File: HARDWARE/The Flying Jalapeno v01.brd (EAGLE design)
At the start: 73.7 x 52.1 mm, 80 parts, among them J1 ., J2 7V, Q1 16MHZ, Q3 P-Channel MOSFET, U2 ATMEGA328P_TQFP

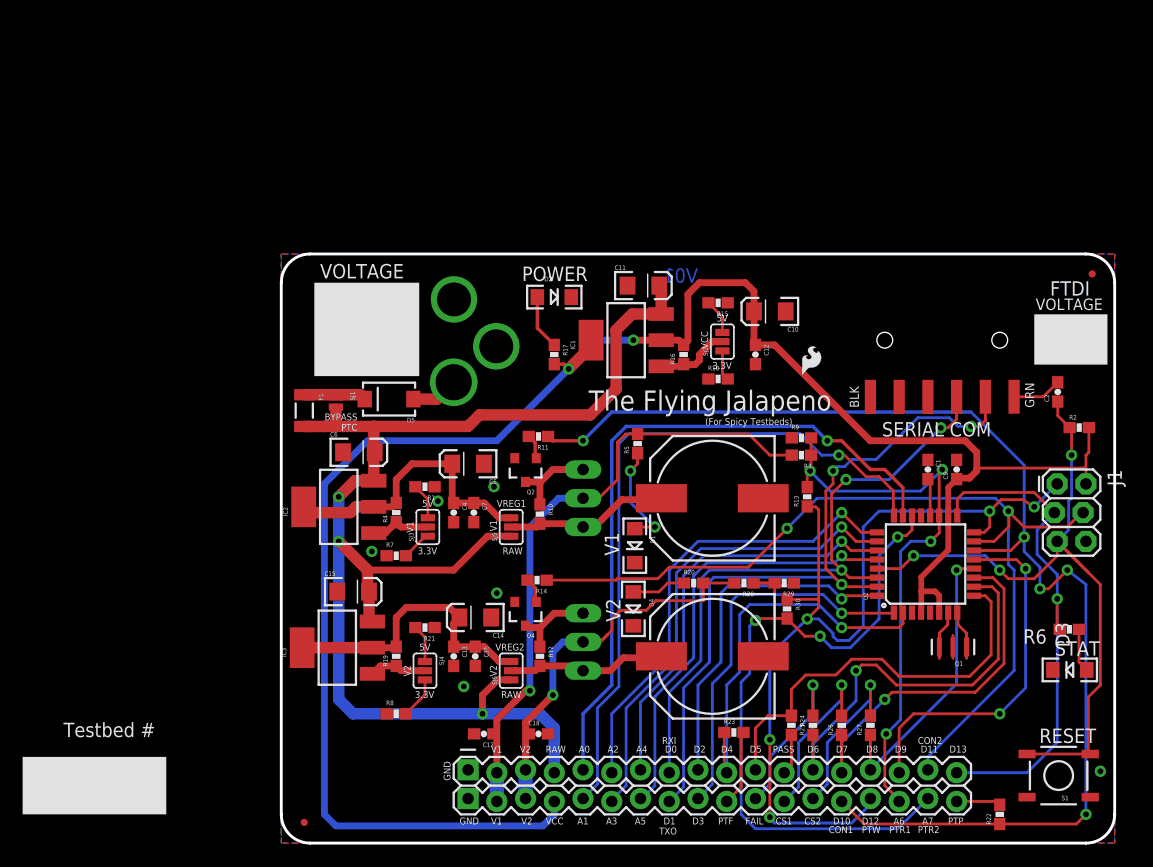
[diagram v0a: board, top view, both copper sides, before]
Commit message: Moved to Mega2560 and 2x30 2mm connector
device and packages for the 2x30 connector all live in the "local"
sparkfun.lbr for now. I will push to testing.lbr soon.
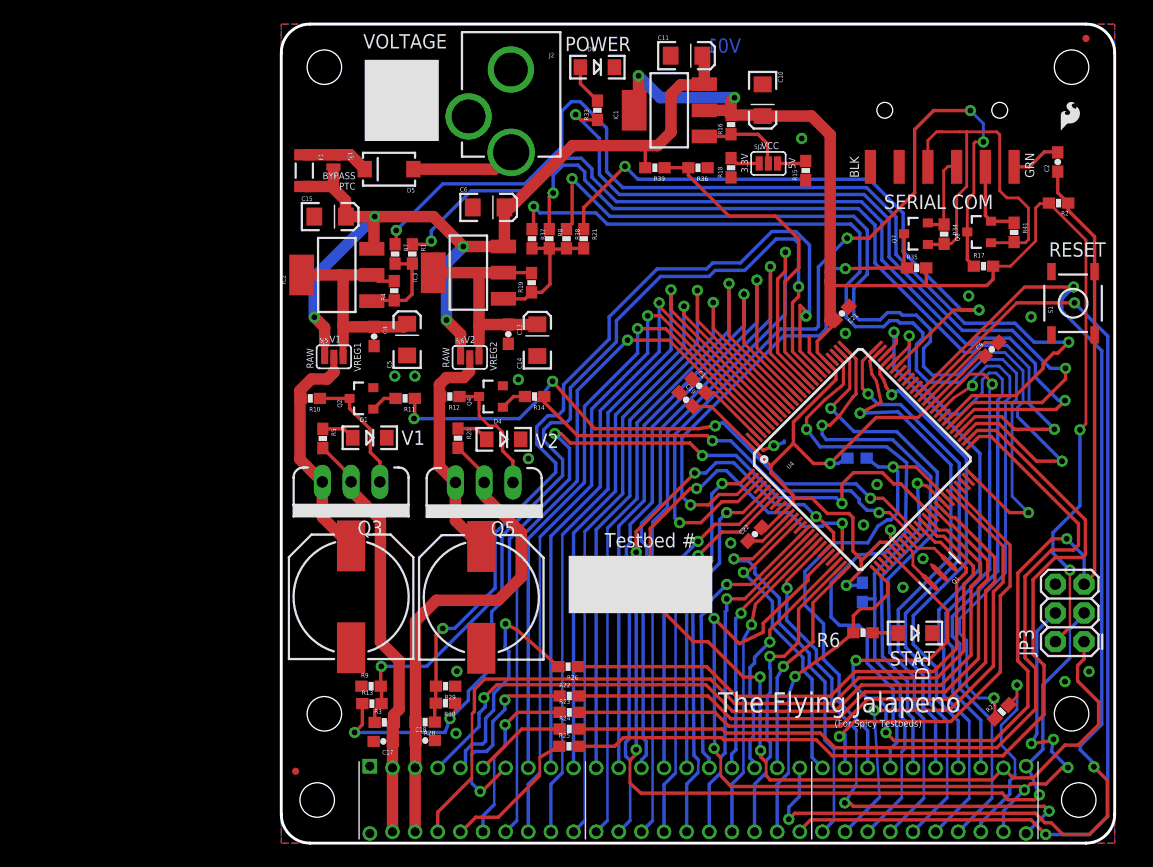
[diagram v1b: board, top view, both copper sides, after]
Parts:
- removed C12, C16, C7: 0.1uF, SparkFun-Capacitors:0603-CAP
- removed D2: RED, SparkFun-LED:LED-1206
- removed J1: ., SparkFun:2X3_LOCK
- removed JP1: FTDI Basic, SparkFun-Connectors:1X06-SMD
- removed JP4: FLYING_JALAPENO, Testing:FLYING_JALAPENO
- removed SJ3, SJ4: (no value), SparkFun-Passives:PAD-JUMPER-3-2OF3_NC_BY_PASTE_YES_SILK_FULL_BOX
- removed U2: ATMEGA328P_TQFP, SparkFun-DigitalIC:TQFP32-08
- added C19, C21, C22: 0.1uF, SparkFun-Capacitors:0603-CAP
- added D6: RED, SparkFun-LED:LED-1206
- added JP15: FTDI, SparkFun:1X06-SMD
- added JP3: AVR_SPI_PRG_6PTH, SparkFun:2X3
- added JP6: FLYING_JALAPENO_V2FEMALE, SparkFun:FLYING_JALAPENO_V2_F
- added Q6, Q7: 200mA/50V, SparkFun-DiscreteSemi:SOT23-3
- added R31, R32: DNP, SparkFun-Resistors:0603-RES
- added R33: 390, SparkFun-Resistors:0603-RES
- added R34, R35, R36, R41: 10K, SparkFun-Resistors:0603-RES
- added R37, R38: ?, SparkFun-Resistors:0603-RES
- added R39: 100k, SparkFun-Resistors:0603-RES
- added STANDOFF1, STANDOFF2, STANDOFF3, STANDOFF4: STAND-OFFTIGHT, SparkFun-Electromechanical:STAND-OFF-TIGHT
- added U4: ATMEGA2560AU, SparkFun:TQFP100
- R17: value 390 -> 10K
- moved LOGO4 53.2 mm to (43.2, 47.0)
- moved R8 44.1 mm to (23.7, 53.4), turned to 270 degrees
- moved R9 43.9 mm to (7.94, 13.9)
- moved R3 43.8 mm to (9.11, 10.7), turned to 0 degrees
- moved R13 42.6 mm to (8.01, 12.3), turned to 0 degrees
- moved S1 41.8 mm to (70.0, 47.7), turned to 90 degrees
- moved R22 39.5 mm to (25.5, 13.0), turned to 0 degrees
- moved R17 38.7 mm to (62.1, 51.0), turned to 0 degrees
- moved R21 37.1 mm to (26.7, 53.4), turned to 270 degrees
- moved R19 35.1 mm to (22.1, 49.5)
- moved IC3 35.1 mm to (16.5, 50.4)
- moved C15 33.2 mm to (4.32, 55.4)
- moved C3 33.1 mm to (6.17, 21.8), turned to 90 degrees
- moved LOGO3 31.4 mm to (68.6, 62.6)
- moved R30 31.3 mm to (14.5, 12.4), turned to 180 degrees
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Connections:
- removed net A6/PRETESTREAD_V1: JP4.34, R13.2, R3.1, R9.2, U2.19
- removed net A7/PRETESTREAD_V2: JP4.35, R28.1, R29.2, R30.2, U2.22
- removed net CAPSENSE1: JP4.30, R26.2
- removed net CAPSENSE2: JP4.31, R27.2
- removed net D10/CONT1: JP4.32, R11.1, R22.1, U2.14
- removed net D11/CONT2: J1.4, JP4.17, R14.1, U2.15
- removed net D12/PRETEST-WRITE: J1.1, JP4.33, R13.1, R30.1, U2.16
- removed net FAIL: JP4.29, R25.2
- removed net N$4 (its old number): IC2.1, R4.1, SJ3.2
- removed net PASS: JP4.12, R24.2
- removed net PT-FAIL: JP4.28, R23.2
- removed net PT-PASS: JP4.36, R22.2
- removed net RX: JP1.2, JP4.26, U2.31
- removed net SCK: J1.3, JP4.18, R6.1, U2.17
- removed net TX: JP1.3, JP4.8, U2.30
- new net 31/CAPRETURN2: R27.1, U4.59
- new net 33/V1_3.3V: R7.1, U4.57
- new net 34/RAW_PASS_LED: R33.1, U4.56
- new net 35/V1_5V: R1.1, U4.55
- new net 36/V2_3.3V: R8.1, U4.54
- new net 37/V2_3.7V: R38.1, U4.53
- new net 38/V2_4.2V: R37.1, U4.50
- new net 39/V2_5V: R21.1, U4.70
- new net 40/FAIL: R25.2, U4.52
- new net 41/PASS: R24.2, U4.51
- new net 42/PT_FAIL: R23.2, U4.42
- new net 43/PT_PASS: R22.2, U4.41
- new net 44/PT_CTRL: R13.1, R30.1, U4.40
- new net 45/CAPSENSE1: JP6.4, U4.39
- new net 46/CAPSENSE2: JP6.34, U4.38
- new net 47/CAPRETURN1: R26.1, U4.37
- new net 48/PWR_CTRL1: R11.1, U4.36
- new net 49/PWR_CTRL2: R14.1, U4.35
- new net A10: JP6.42, U4.87
- new net A11: JP6.13, U4.86
- new net A12: JP6.43, U4.85
- new net A13/RAW_READ: R36.2, R39.1, U4.84
- new net A14/PT_READ_V1: R13.2, R3.1, R9.2, U4.83
- new net A15/PT_READ_V2: R28.1, R29.2, R30.2, U4.82
- new net A6: JP6.40, U4.91
- new net A7: JP6.11, U4.90
- new net A8: JP6.41, U4.89
- new net A9: JP6.12, U4.88
- new net D10: JP6.18, U4.23
- new net D11: JP6.48, U4.24
- new net D12: JP6.19, U4.25
- new net D13: JP6.49, R6.1, U4.26
- new net D22: JP6.24, U4.78
- new net D23: JP6.54, U4.77
- new net D24: JP6.25, U4.76
- new net D25: JP6.55, U4.75
- new net D26: JP6.26, U4.74
- new net D27: JP6.56, U4.73
- new net D28: JP6.27, U4.72
- new net D29: JP6.57, U4.71
- new net D30: JP6.28, U4.60
- new net FTDI_VCC: JP15.4, Q6.1, Q7.1, R34.2, R41.2
- new net N$25: D6.A, R33.2
- new net N$26: JP15.2, Q6.2, R41.1
- new net N$7: JP6.36, R23.1
- new net N$73: Q1.3, U4.33
- new net N$74: Q1.1, U4.34
- new net PB0: JP6.60, U4.19
- new net PB1: JP3.3, JP6.30, U4.20
- new net PB2: JP3.4, JP6.59, U4.21
- new net PB3: JP3.1, JP6.29, U4.22
- new net PC5: U4.58
- new net RX0: Q7.3, R35.1, U4.2
- new net RX1: JP6.52, U4.45
- new net RX2: JP6.51, U4.12
- new net RX3: JP6.50, U4.63
- new net SCL: JP6.53, R32.1, U4.43
- new net SDA: JP6.23, R31.1, U4.44
- new net TX0: Q6.3, R17.1, U4.3
- new net TX1: JP6.22, U4.46
- new net TX2: JP6.21, U4.13
- new net TX3: JP6.20, U4.64
- net A0: now also JP6.37, U4.97; no longer JP4.5, U2.23
- net A1: now also JP6.8, U4.96; no longer JP4.23, U2.24
- net A2: now also JP6.38, U4.95; no longer JP4.6, U2.25
- net A3: now also JP6.9, U4.94; no longer JP4.24, U2.26
- net A4: now also JP6.39, U4.93; no longer JP4.7, U2.27
- net A5: now also JP6.10, U4.92; no longer JP4.25, U2.28
- net AREF: now also U4.98; no longer U2.20
- net D2: now also JP6.14, U4.6; no longer JP4.9, U2.32
- net D3: now also JP6.44, U4.7; no longer JP4.27, U2.1
- net D4: now also JP6.15, U4.1; no longer JP4.10, R23.1, U2.2
- net D5: now also JP6.45, U4.5; no longer JP4.11, R24.1, U2.9
- net D6: now also JP6.16, U4.15; no longer JP4.13, R25.1, U2.10
- net D7: now also JP6.46, U4.16; no longer JP4.14, R26.1, U2.11
- net D8: now also JP6.17, U4.17; no longer JP4.15, R27.1, U2.12
- net D9: now also JP6.47, U4.18; no longer JP4.16, U2.13
- net DTR: now also JP15.1; no longer JP1.1
- net GND: now also C19.1, C21.1, C22.1, D6.C, JP15.5, JP15.6, JP3.6, JP6.1, JP6.31, R36.1, U4.11, U4.32, U4.62, U4.81, U4.99; no longer C12.2, C16.2, C7.2, D2.C, J1.6, JP1.5, JP1.6, JP4.1, JP4.19, R1.1, R21.1, R7.1, R8.1, U2.21, U2.3, U2.5
- net N$1: now also JP6.5, R26.2; no longer Q1.1, U2.8
- net N$10: now also R21.2, R37.2, R38.2, R8.2; no longer SJ4.2
- net N$16: now also JP15.3, Q7.2, R34.1; no longer D2.A, R17.1
- net N$19: now also JP6.6, R24.1; no longer R21.2, SJ4.1
- net N$2: now also JP6.58, R27.2; no longer Q1.3, U2.7
- net N$20: now also JP6.35, R25.1; no longer R8.2, SJ4.3
- net N$21: no longer C7.1
- net N$6: now also JP6.7, R22.1; no longer R7.2, SJ3.1
- net N$9: now also IC2.1, R4.1, R7.2; no longer SJ3.3
- net RAW: now also R39.2; no longer JP4.4
- net RESET: now also JP3.5, U4.30; no longer J1.5, U2.29
- net V1: now also JP6.2, JP6.32; no longer JP4.2, JP4.20
- net V2: now also JP6.3, JP6.33; no longer JP4.21, JP4.3
- net VCC: now also C19.2, C21.2, C22.2, JP3.2, R31.2, R32.2, R35.2, U4.10, U4.100, U4.31, U4.61, U4.80; no longer C12.1, J1.2, JP4.22, U2.18, U2.4, U2.6
- net VREG2OUT: no longer C16.1
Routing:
- net D10/CONT1: track 109.9 -> 0.00 mm, vias 5 -> 0
- net TX3: track 0.00 -> 102.6 mm, vias 0 -> 3
- net PB1: track 0.00 -> 102.5 mm, vias 0 -> 5
- net 33/V1_3.3V: track 0.00 -> 94.0 mm, vias 0 -> 2
- net PB3: track 0.00 -> 93.2 mm, vias 0 -> 4
- net RX3: track 0.00 -> 92.2 mm, vias 0 -> 2
- net 35/V1_5V: track 0.00 -> 84.4 mm, vias 0 -> 2
- net 44/PT_CTRL: track 0.00 -> 83.5 mm, vias 0 -> 5
- net D11/CONT2: track 83.2 -> 0.00 mm, vias 2 -> 0
- net 37/V2_3.7V: track 0.00 -> 82.8 mm, vias 0 -> 2
- net PB2: track 0.00 -> 82.8 mm, vias 0 -> 6
- net 38/V2_4.2V: track 0.00 -> 81.1 mm, vias 0 -> 2
- net A14/PT_READ_V1: track 0.00 -> 81.0 mm, vias 0 -> 2
- net D12/PRETEST-WRITE: track 80.8 -> 0.00 mm, vias 5 -> 0
- net A15/PT_READ_V2: track 0.00 -> 80.2 mm, vias 0 -> 2
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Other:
- board size 73.7 x 52.1 mm -> 73.7 x 72.4 mm
- board text removed: "FTDI"

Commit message: trace cleanup
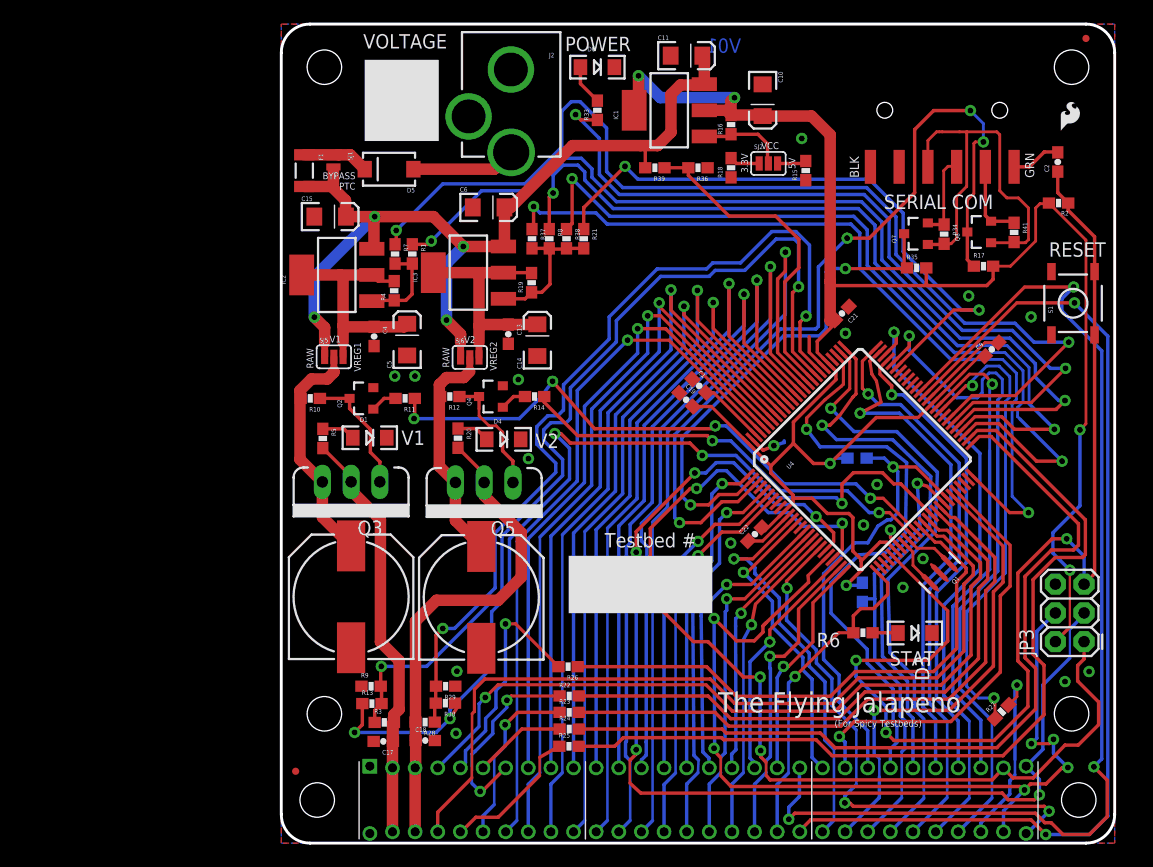
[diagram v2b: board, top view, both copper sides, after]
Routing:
- net 37/V2_3.7V: track 82.8 -> 73.7 mm
- net 38/V2_4.2V: track 81.1 -> 72.1 mm
- net D29: track 63.0 -> 60.1 mm
- net SDA: track 43.1 -> 40.7 mm
- net A15/PT_READ_V2: track 80.2 -> 78.3 mm
- net D26: track 47.2 -> 45.4 mm
- net D28: track 43.9 -> 42.0 mm
- net D25: track 52.8 -> 51.0 mm
- net TX3: track 102.6 -> 101.6 mm
- net D22: track 52.9 -> 51.9 mm
- net N$2: track 17.3 -> 16.3 mm
- net 35/V1_5V: track 84.4 -> 83.4 mm
- net RESET: track 101.3 -> 100.6 mm
- net N$6: track 18.3 -> 17.6 mm
- net N$1: track 21.2 -> 20.7 mm
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
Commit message: Modified Capsense pad device to use only 1 pin/pad
I realized that I don't need the usual two lines for capsense buttons on
this (SEND/RETURN). Because the resistors are going to live on the
board, then the "button" on the testbed is only an extension of one net.
Updated library devices to reflect this correction.
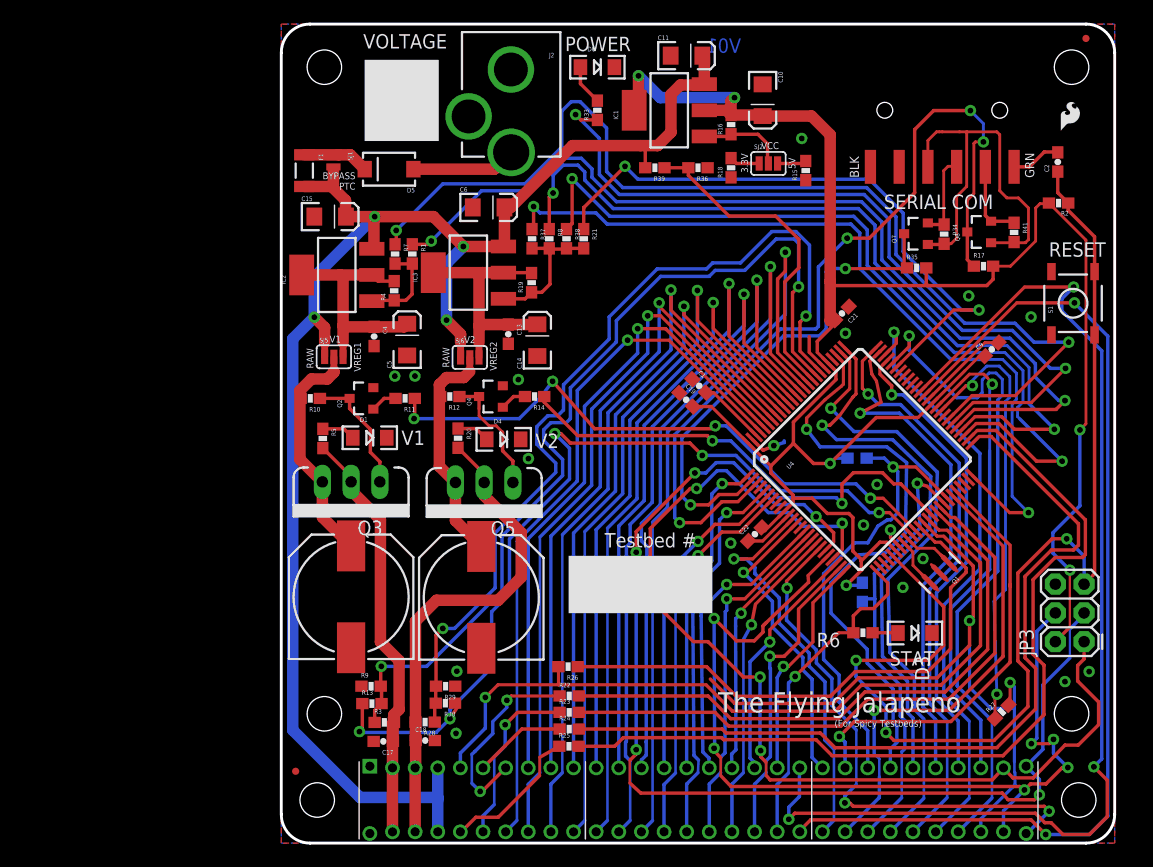
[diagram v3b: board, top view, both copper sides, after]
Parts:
- R38: value ? -> 470
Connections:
- removed net N$1: JP6.5, R26.2
- removed net N$2: JP6.58, R27.2
- net 45/CAPSENSE1: now also JP6.5, R26.2; no longer JP6.4
- net 46/CAPSENSE2: now also JP6.58, R27.2; no longer JP6.34
- net RAW: now also JP6.34, JP6.4
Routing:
- net RAW: track 83.6 -> 141.8 mm
- net N$1: track 20.7 -> 0.00 mm, vias 1 -> 0
- net N$2: track 16.3 -> 0.00 mm, vias 1 -> 0
- net 46/CAPSENSE2: track 74.1 -> 66.3 mm, vias 0 -> 2
- net 31/CAPRETURN2: track 42.1 -> 39.3 mm
- net 45/CAPSENSE1: track 69.1 -> 69.8 mm
- net 44/PT_CTRL: track 83.2 -> 82.5 mm

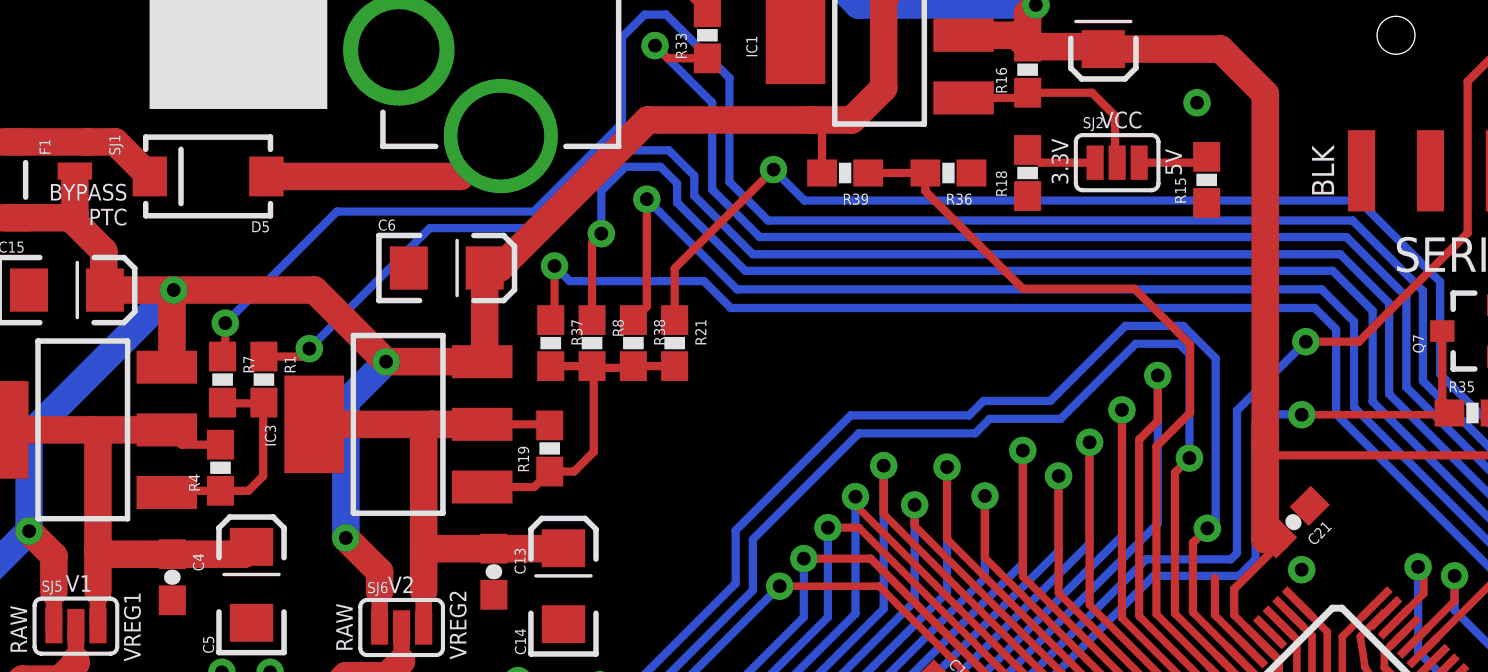
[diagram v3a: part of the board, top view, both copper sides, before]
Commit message: finalized resistor values on lipo fake out vreg
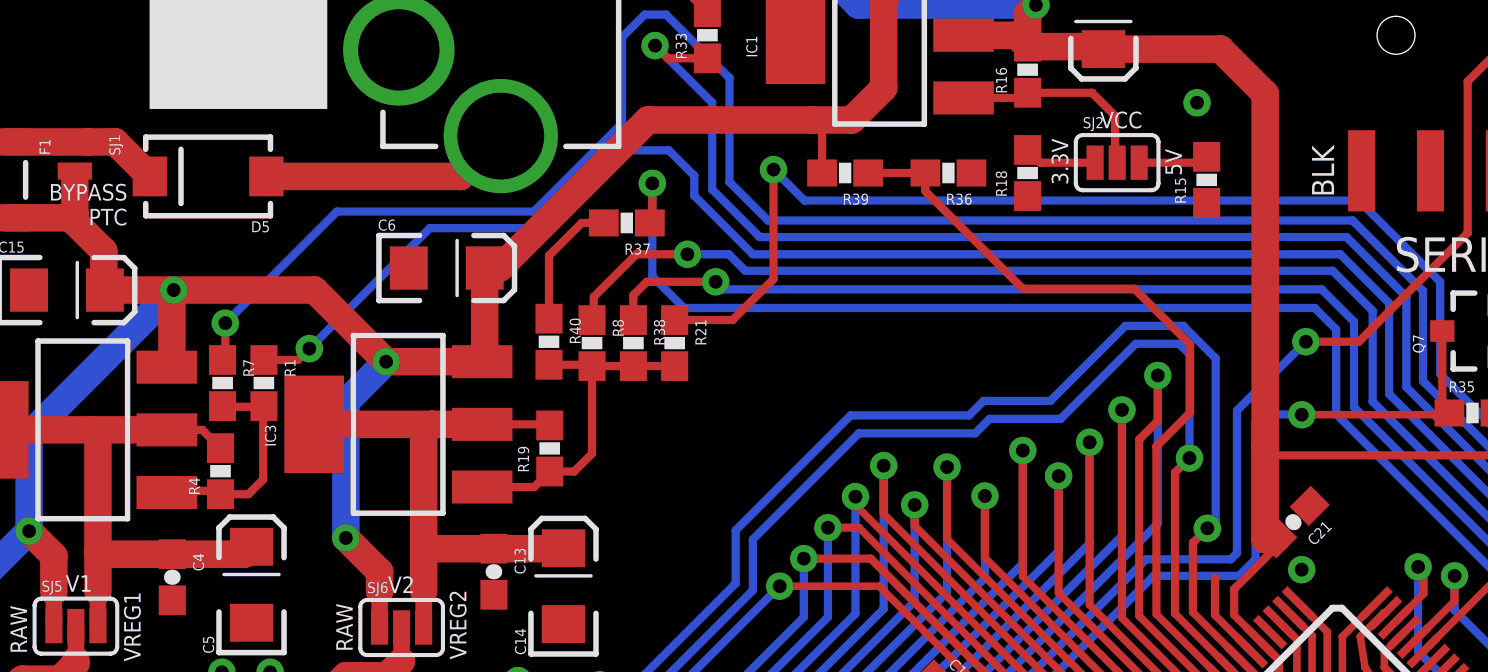
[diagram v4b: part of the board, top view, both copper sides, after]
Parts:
- added R40: 470, SparkFun-Resistors:0603-RES
- R37: value ? -> 100
- moved R37 5.25 mm to (25.0, 57.8), turned to 180 degrees
- moved R1 0.13 mm to (11.6, 51.9)
- moved R4 0.13 mm to (9.98, 48.7)
- moved R7 0.13 mm to (10.1, 51.9)
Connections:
- new net N$1: R37.2, R40.1
- net N$10: now also R40.2; no longer R37.2
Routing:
- net 36/V2_3.3V: track 72.8 -> 67.6 mm
- net N$1: track 0.00 -> 4.84 mm
- net 37/V2_3.7V: track 73.7 -> 69.4 mm
- net 39/V2_5V: track 55.0 -> 56.3 mm
- net 38/V2_4.2V: track 72.1 -> 71.2 mm
